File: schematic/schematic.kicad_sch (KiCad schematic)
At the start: 3 parts

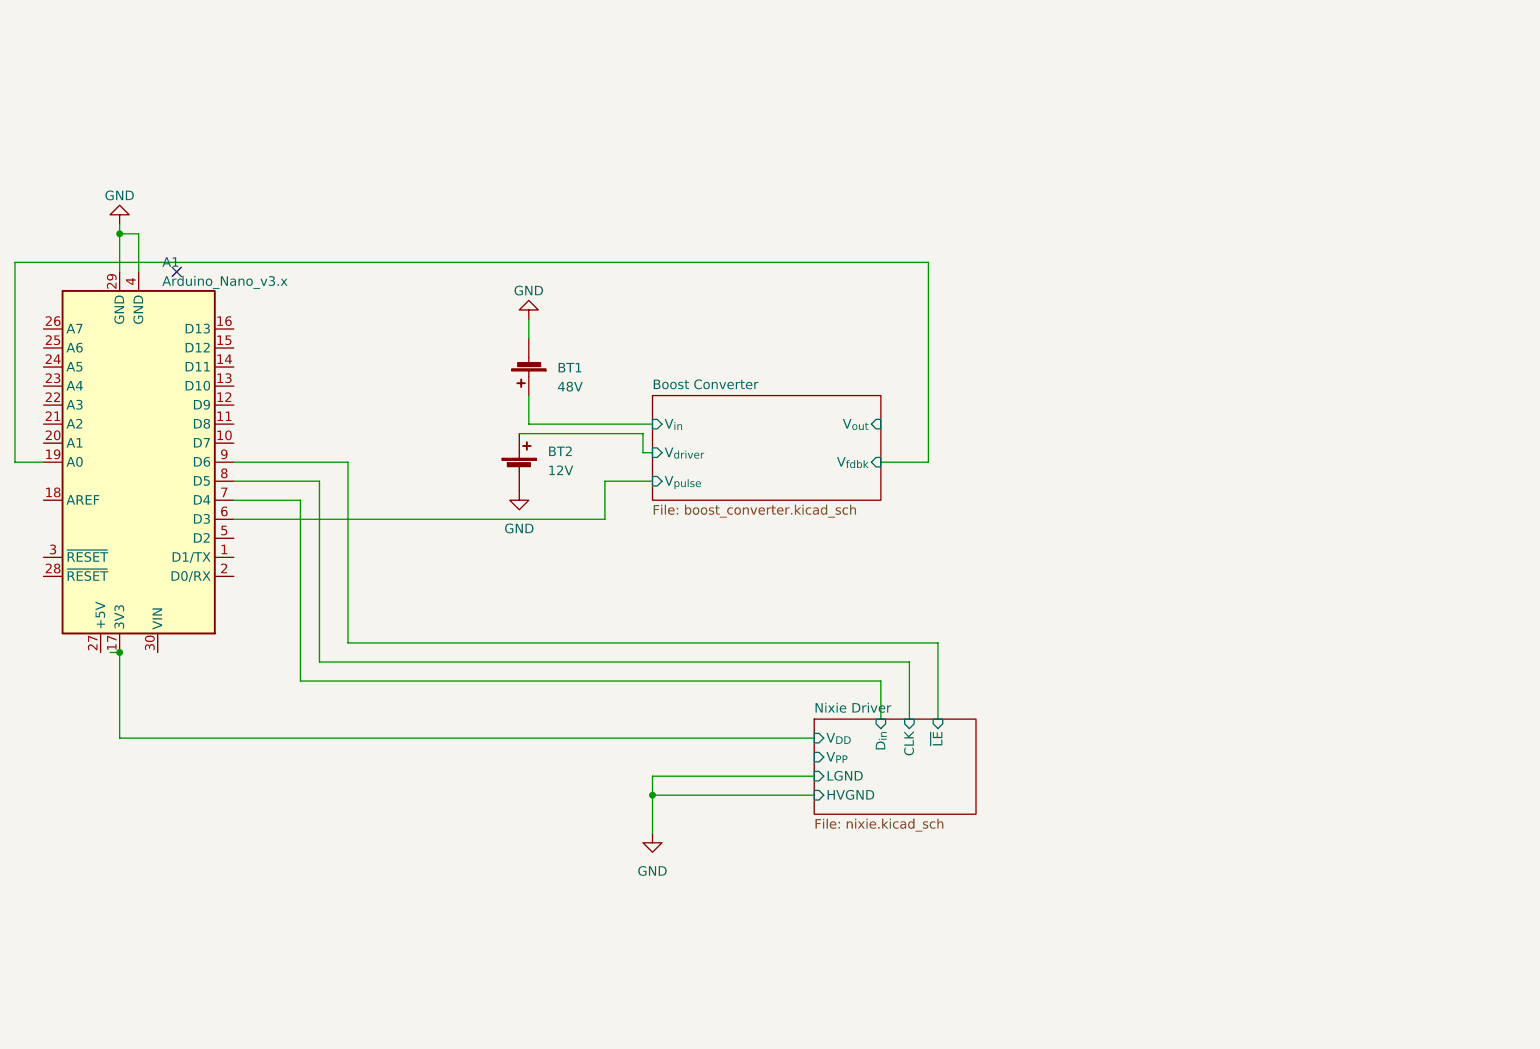
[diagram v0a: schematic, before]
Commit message: Add buck converter to schematic
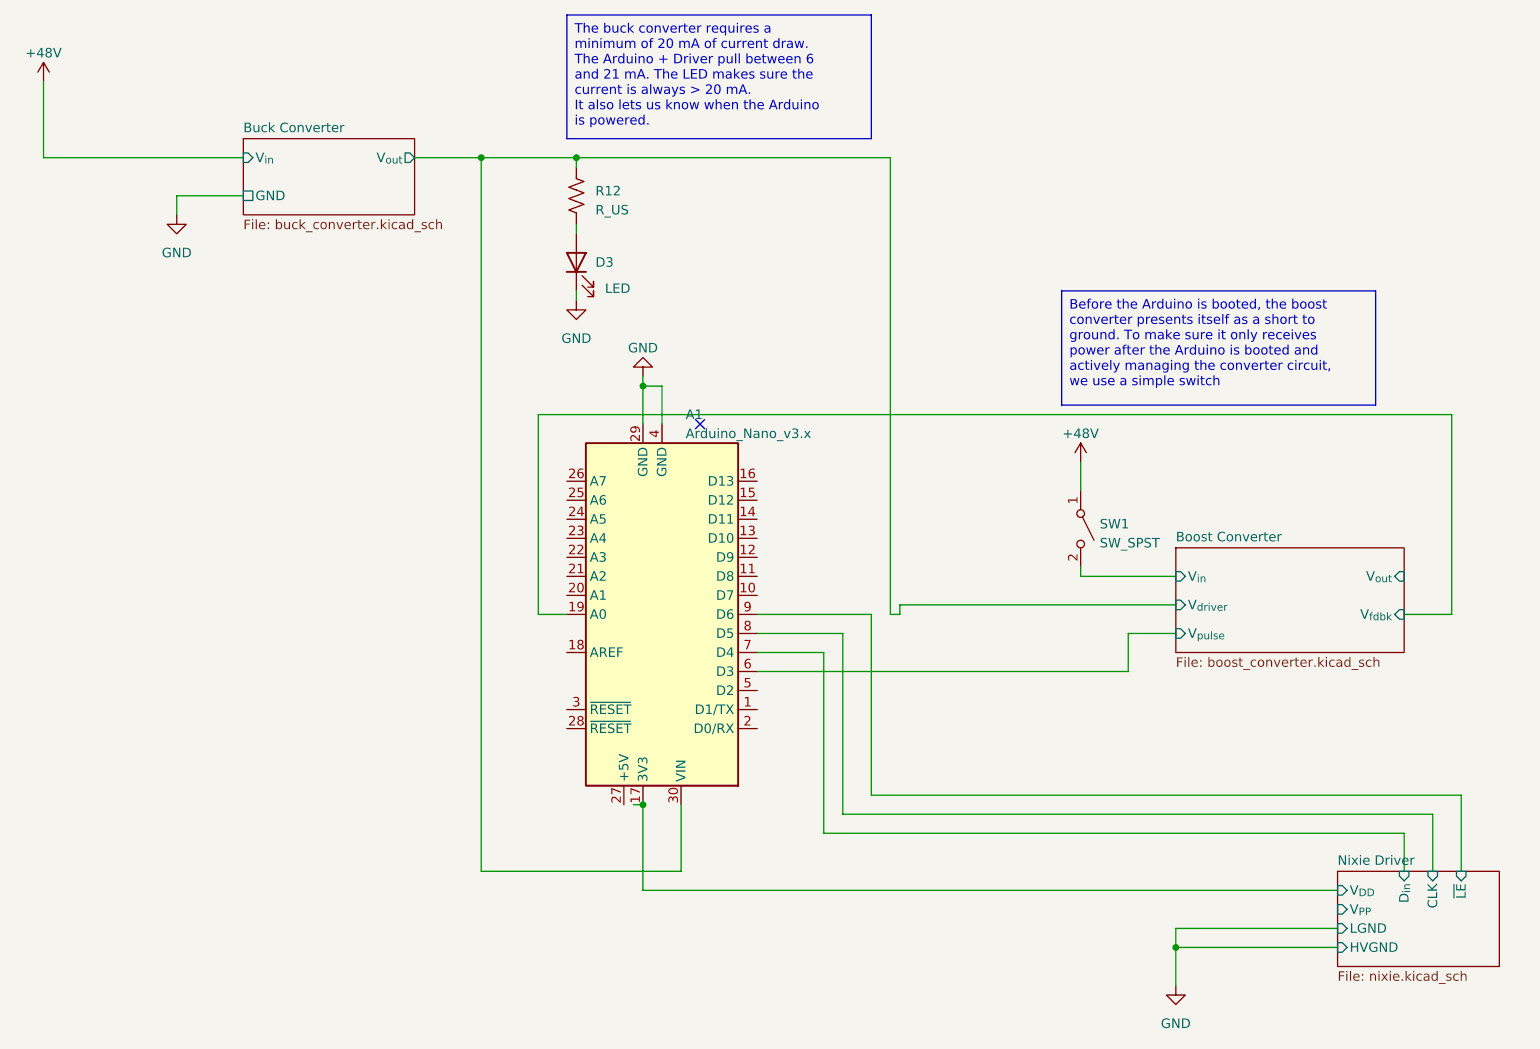
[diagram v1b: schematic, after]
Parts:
- removed BT1: 48V, symbol Device:Battery_Cell
- removed BT2: 12V, symbol Device:Battery_Cell
- added D3: LED, symbol Device:LED
- added R12: R_US, symbol Device:R_US
- added SW1: SW_SPST, symbol Switch:SW_SPST
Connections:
- net Boost Converter/V_{driver}: now also A1.30 (VIN), R12.1
- net Boost Converter/V_{in}: now also SW1.2 (B)
- net GND: now also D3.1 (K)
- new net: D3.2 (A), R12.2
- new net +48V: SW1.1 (A)
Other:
- added sheet Buck Converter (buck_converter.kicad_sch)
- moved on the sheet: A1
